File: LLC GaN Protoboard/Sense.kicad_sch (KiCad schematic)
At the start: 0 parts

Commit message: Finished schematic
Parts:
- added C10, C9: 1n, Capacitor_SMD:C_0603_1608Metric, symbol Device:C
- added D6, D7: ADS12B3-ASARH, ADS12B3-ASARH:ADS12B3ASARH, symbol ADS12B3-ASARH:ADS12B3-ASARH
- added IC7, IC8: AMC1200SDUBR, SOP254P1040X485-8N, symbol AMC1200SDUBR:AMC1200SDUBR
- added PS1: CME0303S3C, CME0303S3C, symbol CME0303S3C:CME0303S3C
- added R10, R11, R12, R13, R14, R15, R16, R9: 10k, symbol Device:R
- added R17, R18: 20k, symbol Device:R
- added R19: 90k, symbol Device:R
- added R20, R7, R8: 1k, symbol Device:R
- added U2: LM124DR, LM124DR:SOIC127P600X175-14N, symbol LM124DR:LM124DR
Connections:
- new net: IC8.2 (VINP), R19.1, R20.2
- new net +3.3V: IC7.8 (VDD2), IC8.8 (VDD2), PS1.2 (+VIN), R12.2, R17.2, U2.6 (2IN-)
- new net +3.3V_ISO: IC7.1 (VDD1), IC8.1 (VDD1), PS1.4 (+VOUT)
- new net 1IN+: R10.2, R9.1, U2.3 (1IN+)
- new net 1IN-: R11.2, R12.1, U2.2 (1IN-)
- new net 2IN+: R13.2, R16.1, U2.5 (2IN+)
- new net 3IN+: R14.2, R18.1
- new net 3IN-: R15.2, R17.1
- new net ADC_IIN: R9.2, U2.1 (1OUT)
- new net ADC_IOUT: R18.2, U2.8 (3OUT)
- new net ADC_VIN: R16.2, U2.7 (2OUT)
- new net ADC_VOUT: IC8.7 (VOUTP)
- new net GND: C10.2, C9.2, IC7.5 (GND2), IC8.5 (GND2), IC8.6 (VOUTN), PS1.1 (-VIN), R7.2, R8.2, U2.11 (GND)
- new net GND_ISO: IC7.4 (GND1), IC8.3 (VINN), IC8.4 (GND1), PS1.3 (-VOUT), R20.1
- new net INV_HIGH: C9.1, D6.1 (K), R10.1, R13.1, R7.1
- new net INV_LOW: C10.1, D7.1 (K), R11.1, R8.1
- new net INV_SHUNT_HIGH: D6.2 (A)
- new net INV_SHUNT_LOW: D7.2 (A)
- new net IOUT_VOUTN: IC7.6 (VOUTN), R15.1
- new net IOUT_VOUTP: IC7.7 (VOUTP), R14.1
- new net VIN: U2.4 (VCC)
- new net VOUT: R19.2
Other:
- note added: "IIN"
- note added: "IOUT"
- note added: "VOUT"
- note added: "isolated amplifiers"
- note added: "isolated power"
- note added: "supply should go to maximum 30V, input current roughly 6A"

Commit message: Edited schematic
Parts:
- added TP18, TP19, TP20, TP21, TP22, TP23, TP24, TP25, TP26: 5019, 5019:5019, symbol 5019:5019
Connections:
- net +3.3V: now also TP21.1
- net +3.3V_ISO: now also TP20.1
- net ADC_IIN: now also TP25.1
- net ADC_IOUT: now also TP26.1
- net ADC_VIN: now also TP24.1
- net ADC_VOUT: now also TP23.1
- net INV_HIGH: now also TP18.1
- net INV_LOW: now also TP19.1
- net IOUT_HIGH: now reaches IC7.2 (VINP)
- net IOUT_LOW: now reaches IC7.3 (VINN)
- net at IC8.2 (VINP), R19.1, R20.2: now also TP22.1

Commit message: first route
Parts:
- removed TP18, TP19: 5019, 5019:5019, symbol 5019:5019
- IC7, IC8: footprint SOP254P1040X485-8N -> AMC1200SDUBR:SOP254P1040X485-8N
- PS1: footprint CME0303S3C -> CME0303S3C:CME0303S3C
- R10, R11, R12, R13, R14, R15, R16, R17, R18, R7, R8, R9: footprint (none) -> Resistor_SMD:R_0603_1608Metric_Pad0.98x0.95mm_HandSolder
- R19: footprint (none) -> Resistor_THT:R_Axial_Power_L38.0mm_W6.4mm_P45.72mm
- R20: footprint (none) -> Resistor_SMD:R_1210_3225Metric_Pad1.30x2.65mm_HandSolder
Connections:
- net 3IN+: now also U2.10 (3IN+)
- net 3IN-: now also U2.9 (3IN-)
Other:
- moved on the sheet: C10, C9, D6, D7, R7, R8

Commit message: Initial primary side layout
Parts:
- added J3: Conn_01x05_Pin, Connector_PinSocket_2.54mm:PinSocket_1x05_P2.54mm_Vertical, symbol Connector:Conn_01x05_Pin
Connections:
- net +3.3V_ISO: now also J3.1 (Pin_1)
- net GND_ISO: now also J3.2 (Pin_2)
- net IOUT_HIGH: now also J3.3 (Pin_3)
- net IOUT_LOW: now also J3.4 (Pin_4)
- net VINP: now reaches IC8.2 (VINP), R19.1, R20.2, TP22.1
- net VINP: now also J3.5 (Pin_5)
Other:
- moved on the sheet: IC7

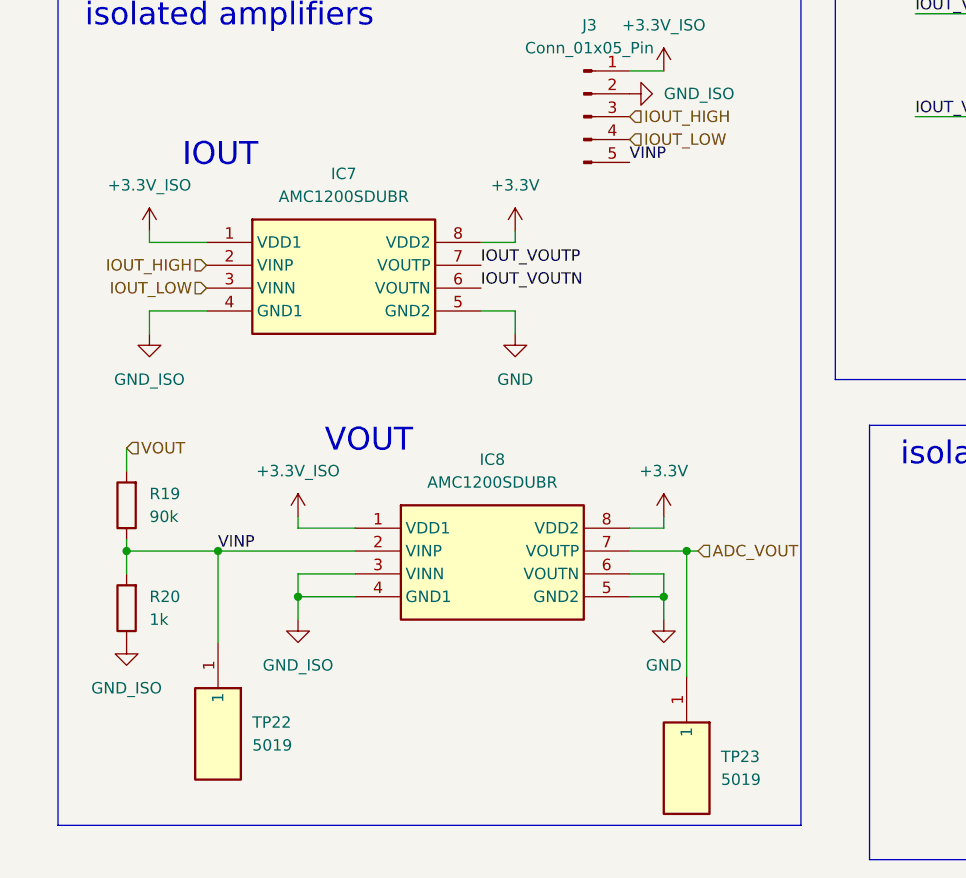
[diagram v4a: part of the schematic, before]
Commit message: Added open spots for soldering
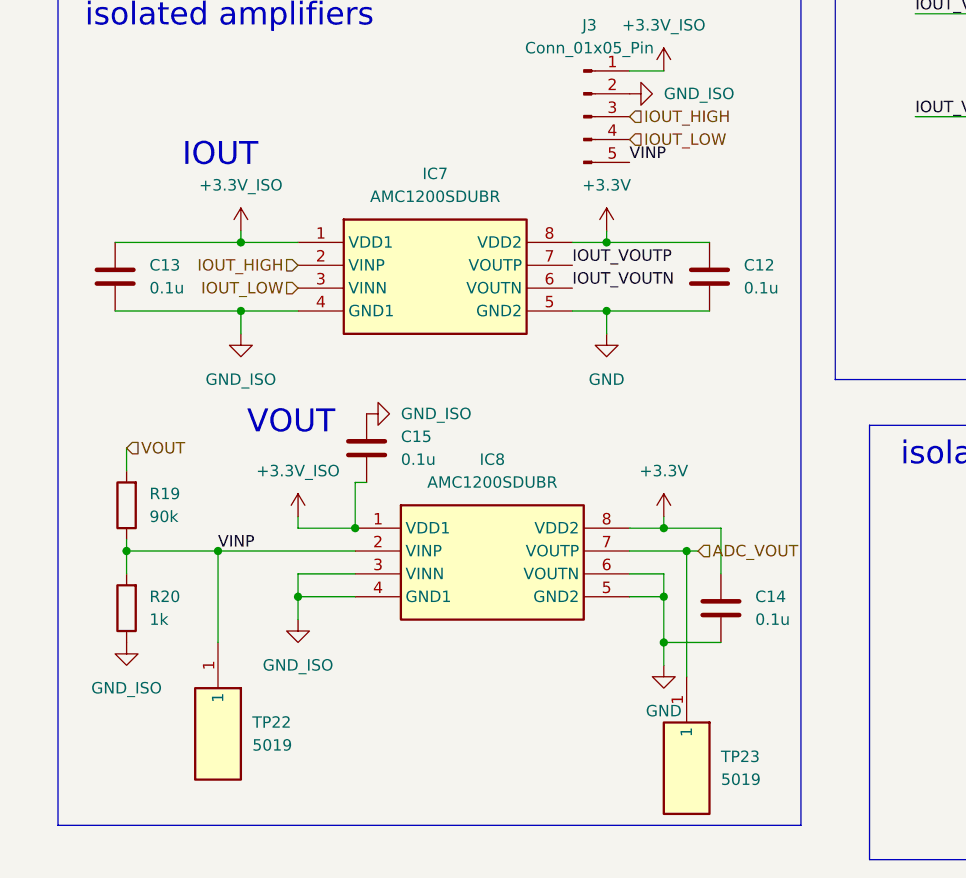
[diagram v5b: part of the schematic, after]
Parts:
- added C12, C13, C14, C15: 0.1u, Capacitor_SMD:C_0603_1608Metric, symbol Device:C
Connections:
- net +3.3V: now also C12.1, C14.1
- net +3.3V_ISO: now also C13.1, C15.2
- net GND: now also C12.2, C14.2
- net GND_ISO: now also C13.2, C15.1
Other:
- moved on the sheet: IC7

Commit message: Added secondary clamp and swapped components
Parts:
- renumbered R19 to MFR-25FRF52-178K
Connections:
- net 3IN+: no longer U2.10 (3IN+)
- net 3IN-: no longer U2.9 (3IN-)
- net ADC_IOUT: now also IC7.7 (VOUTP); no longer R18.2, TP26.1, U2.8 (3OUT)
- net GND: now also IC7.6 (VOUTN)
- net IOUT_VOUTN: no longer names the net of R15.1
- net IOUT_VOUTN: no longer IC7.6 (VOUTN)
- net IOUT_VOUTP: no longer names the net of R14.1
- net IOUT_VOUTP: no longer IC7.7 (VOUTP)
- new net 3OUT: R18.2, TP26.1
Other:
- moved on the sheet: R14, R15, R17
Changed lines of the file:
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@@
 		)
 	)
+	(rectangle
+		(start 121.92 90.17)
+		(end 170.18 138.43)
+		(stroke
+			(width 0)
+			(type default)
+		)
+		(fill
+			(type color)
+			(color 255 0 36 0.2)
+		)
+	)
 	(text "VOUT\n"
 		(exclude_from_sim no)
@@
 	(wire
 		(pts
-			(xy 127 114.3) (xy 130.81 114.3)
+			(xy 137.16 116.84) (xy 140.97 116.84)
 		)
 		(stroke
@@
 	(wire
 		(pts
-			(xy 109.22 102.87) (xy 119.38 102.87)
+			(xy 144.78 40.64) (xy 144.78 46.99)
 		)
 		(stroke
@@
 	(wire
 		(pts
-			(xy 144.78 40.64) (xy 144.78 46.99)
+			(xy 109.22 55.88) (xy 119.38 55.88)
 		)
 		(stroke
@@
 	(wire
 		(pts
-			(xy 109.22 55.88) (xy 119.38 55.88)
+			(xy 144.78 177.8) (xy 144.78 175.26)
 		)
 		(stroke
@@
 	(wire
 		(pts
-			(xy 144.78 177.8) (xy 144.78 175.26)
+			(xy 127 44.45) (xy 130.81 44.45)
 		)
 		(stroke
@@
 	(wire
 		(pts
-			(xy 127 44.45) (xy 130.81 44.45)
+			(xy 74.93 133.35) (xy 74.93 135.89)
 		)
 		(stroke
@@
 	(wire
 		(pts
-			(xy 248.92 91.44) (xy 259.08 91.44)
+			(xy 71.12 133.35) (xy 74.93 133.35)
 		)
 		(stroke
@@
 	(wire
 		(pts
-			(xy 109.22 114.3) (xy 119.38 114.3)
-		)
-		(stroke
-			(width 0)
-			(type default)
-		)
-	)
-	(wire
-		(pts
 			(xy 64.77 60.96) (xy 64.77 59.69)
 		)
@@
 	(wire
 		(pts
-			(xy 127 102.87) (xy 130.81 102.87)
+			(xy 132.08 102.87) (xy 130.81 102.87)
 		)
 		(stroke
@@
 	(wire
 		(pts
-			(xy 208.28 99.06) (xy 213.36 99.06)
-		)
-		(stroke
-			(width 0)
-			(type default)
-		)
-	)
-	(wire
-		(pts
 			(xy 142.24 99.06) (xy 144.78 99.06)
 		)
@@
 	(wire
 		(pts
-			(xy 49.53 59.69) (xy 49.53 60.96)
+			(xy 105.41 102.87) (xy 119.38 102.87)
 		)
 		(stroke
@@
 	(wire
 		(pts
-			(xy 149.86 177.8) (xy 144.78 177.8)
+			(xy 49.53 59.69) (xy 49.53 60.96)
 		)
 		(stroke
@@
 	(wire
 		(pts
-			(xy 40.64 167.64) (xy 46.99 167.64)
+			(xy 149.86 177.8) (xy 144.78 177.8)
 		)
 		(stroke
@@
 	(wire
 		(pts
-			(xy 21.59 162.56) (xy 21.59 165.1)
+			(xy 40.64 167.64) (xy 46.99 167.64)
 		)
 		(stroke
@@
 	(wire
 		(pts
-			(xy 124.46 130.81) (xy 130.81 130.81)
+			(xy 21.59 162.56) (xy 21.59 165.1)
 		)
 		(stroke
@@
 	(wire
 		(pts
-			(xy 39.37 59.69) (xy 49.53 59.69)
+			(xy 134.62 133.35) (xy 140.97 133.35)
 		)
 		(stroke
@@
 	(wire
 		(pts
-			(xy 170.18 73.66) (xy 179.07 73.66)
+			(xy 39.37 59.69) (xy 49.53 59.69)
 		)
 		(stroke
@@
 	(wire
 		(pts
-			(xy 208.28 96.52) (xy 213.36 96.52)
+			(xy 170.18 73.66) (xy 179.07 73.66)
 		)
 		(stroke
@@
 	(wire
 		(pts
-			(xy 130.81 121.92) (xy 130.81 130.81)
+			(xy 140.97 124.46) (xy 140.97 133.35)
 		)
 		(stroke
@@
 	)
 	(label "3IN-"
-		(at 208.28 99.06 0)
-		(effects
-			(font
-				(size 1.27 1.27)
-			)
-			(justify left bottom)
-		)
-	)
-	(label "3IN-"
-		(at 130.81 114.3 0)
+		(at 140.97 116.84 0)
 		(effects
 			(font
@@
 	)
 	(label "IOUT_VOUTP"
-		(at 109.22 102.87 0)
+		(at 105.41 102.87 0)
 		(effects
 			(font
@@
 	)
 	(label "IOUT_VOUTN"
-		(at 109.22 114.3 0)
-		(effects
-			(font
-				(size 1.27 1.27)
-			)
-			(justify left bottom)
-		)
-	)
-	(label "3OUT"
-		(at 248.92 91.44 0)
+		(at 106.68 114.3 0)
 		(effects
 			(font
@@
 		)
 	)
-	(label "3IN+"
-		(at 208.28 96.52 0)
-		(effects
-			(font
-				(size 1.27 1.27)
-			)
-			(justify left bottom)
-		)
-	)
 	(label "2IN+"
 		(at 208.28 91.44 0)
@@
 	(hierarchical_label "ADC_IOUT"
 		(shape input)
-		(at 259.08 91.44 0)
+		(at 119.38 102.87 90)
 		(effects
 			(font
@@
 	(symbol
 		(lib_id "Device:R")
-		(at 123.19 102.87 90)
+		(at 128.27 102.87 90)
 		(unit 1)
 		(body_style 1)
@@
 		(fields_autoplaced yes)
 		(property "Reference" "R14"
-			(at 123.19 96.52 90)
+			(at 128.27 96.52 90)
 			(show_name no)
 			(do_not_autoplace no)
@@
 		)
 		(property "Value" "10k"
-			(at 123.19 99.06 90)
+			(at 128.27 99.06 90)
 			(show_name no)
 			(do_not_autoplace no)
@@
 		)
 		(property "Footprint" "Resistor_SMD:R_0603_1608Metric_Pad0.98x0.95mm_HandSolder"
-			(at 123.19 104.648 90)
+			(at 128.27 104.648 90)
 			(hide yes)
 			(show_name no)
@@
 		)
 		(property "Datasheet" ""
-			(at 123.19 102.87 0)
+			(at 128.27 102.87 0)
 			(hide yes)
 			(show_name no)
@@
 		)
 		(property "Description" "Resistor"
-			(at 123.19 102.87 0)
+			(at 128.27 102.87 0)
 			(hide yes)
 			(show_name no)
@@
 		(dnp no)
 		(fields_autoplaced yes)
-		(property "Reference" "R19"
+		(property "Reference" "MFR-25FRF52-178K"
 			(at 24.13 156.2099 0)
 			(show_name no)
@@
 			(project "LLC GaN Protoboard"
 				(path "/07813ae8-ed9f-4173-b5dd-dce781eafd3c/634a37ef-f9d6-4c09-887c-f65d5550ff69"
-					(reference "R19")
+					(reference "MFR-25FRF52-178K")
 					(unit 1)
 				)
@@
 	(symbol
 		(lib_id "Device:R")
-		(at 123.19 114.3 90)
+		(at 133.35 116.84 90)
 		(unit 1)
 		(body_style 1)
@@
 		(fields_autoplaced yes)
 		(property "Reference" "R15"
-			(at 123.19 107.95 90)
+			(at 133.35 110.49 90)
 			(show_name no)
 			(do_not_autoplace no)
@@
 		)
 		(property "Value" "10k"
-			(at 123.19 110.49 90)
+			(at 133.35 113.03 90)
 			(show_name no)
 			(do_not_autoplace no)
@@
 		)
 		(property "Footprint" "Resistor_SMD:R_0603_1608Metric_Pad0.98x0.95mm_HandSolder"
-			(at 123.19 116.078 90)
+			(at 133.35 118.618 90)
 			(hide yes)
 			(show_name no)
@@
 		)
 		(property "Datasheet" ""
-			(at 123.19 114.3 0)
+			(at 133.35 116.84 0)
 			(hide yes)
 			(show_name no)
@@
 		)
 		(property "Description" "Resistor"
-			(at 123.19 114.3 0)
+			(at 133.35 116.84 0)
 			(hide yes)
 			(show_name no)
@@
 	(symbol
 		(lib_id "Device:R")
-		(at 130.81 118.11 0)
+		(at 140.97 120.65 0)
 		(unit 1)
 		(body_style 1)
@@
 		(fields_autoplaced yes)
 		(property "Reference" "R17"
-			(at 133.35 116.8399 0)
+			(at 143.51 119.3799 0)
 			(show_name no)
 			(do_not_autoplace no)
@@
 		)
 		(property "Value" "20k"
-			(at 133.35 119.3799 0)
+			(at 143.51 121.9199 0)
 			(show_name no)
 			(do_not_autoplace no)
@@
 		)
 		(property "Footprint" "Resistor_SMD:R_0603_1608Metric_Pad0.98x0.95mm_HandSolder"
-			(at 129.032 118.11 90)
+			(at 139.192 120.65 90)
 			(hide yes)
 			(show_name no)
@@
 		)
 		(property "Datasheet" ""
-			(at 130.81 118.11 0)
+			(at 140.97 120.65 0)
 			(hide yes)
 			(show_name no)
@@
 		)
 		(property "Description" "Resistor"
-			(at 130.81 118.11 0)
+			(at 140.97 120.65 0)
 			(hide yes)
 			(show_name no)
@@
 	(symbol
 		(lib_id "power:+5V")
-		(at 124.46 130.81 0)
+		(at 134.62 133.35 0)
 		(unit 1)
 		(body_style 1)
@@
 		(fields_autoplaced yes)
 		(property "Reference" "#PWR036"
-			(at 124.46 134.62 0)
+			(at 134.62 137.16 0)
 			(hide yes)
 			(show_name no)
@@
 		)
 		(property "Value" "+3.3V"
-			(at 124.46 125.73 0)
+			(at 134.62 128.27 0)
 			(show_name no)
 			(do_not_autoplace no)
@@
 		)
 		(property "Footprint" ""
-			(at 124.46 130.81 0)
+			(at 134.62 133.35 0)
 			(hide yes)
 			(show_name no)
@@
 		)
 		(property "Datasheet" ""
-			(at 124.46 130.81 0)
+			(at 134.62 133.35 0)
 			(hide yes)
 			(show_name no)
@@
 		)
 		(property "Description" "Power symbol creates a global label with name \"+5V\""
-			(at 124.46 130.81 0)
+			(at 134.62 133.35 0)
 			(hide yes)
 			(show_name no)
